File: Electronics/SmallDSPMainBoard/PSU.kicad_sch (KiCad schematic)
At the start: 17 parts, among them J15 Barrel_Jack_Switch

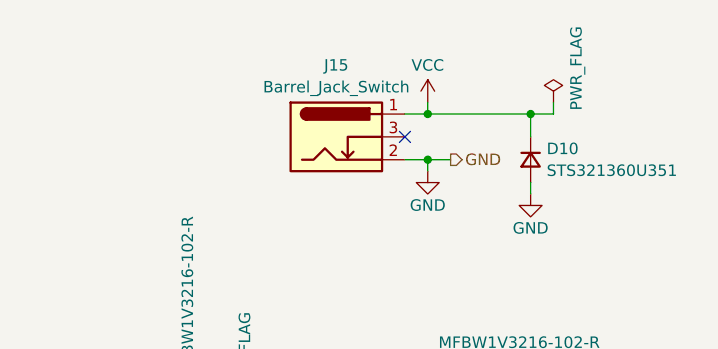
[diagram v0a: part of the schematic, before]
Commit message: Partly finishes layout
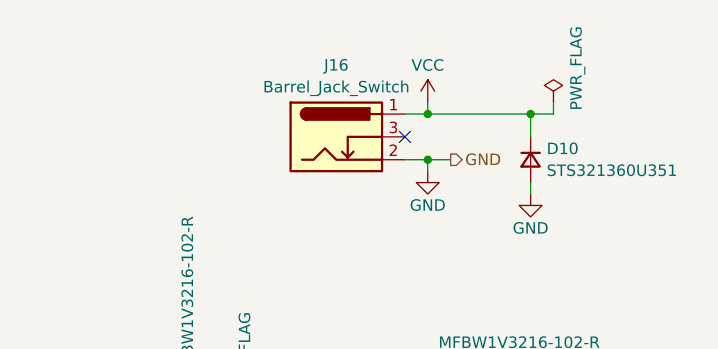
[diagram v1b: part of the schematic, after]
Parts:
- renumbered J15 to J16

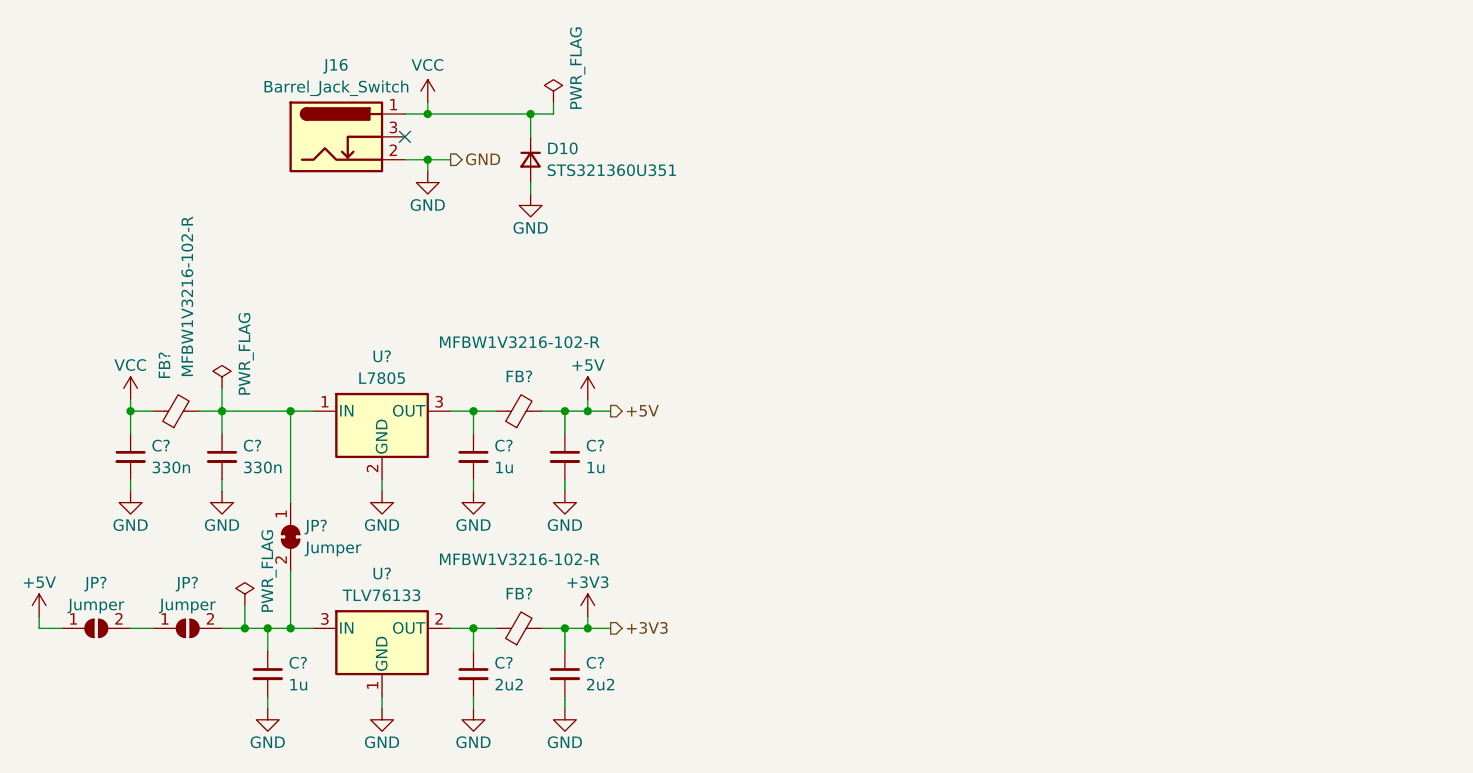
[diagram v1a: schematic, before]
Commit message: Finishes layout of Rev 1.0 and fixes a polarity error in the schematic
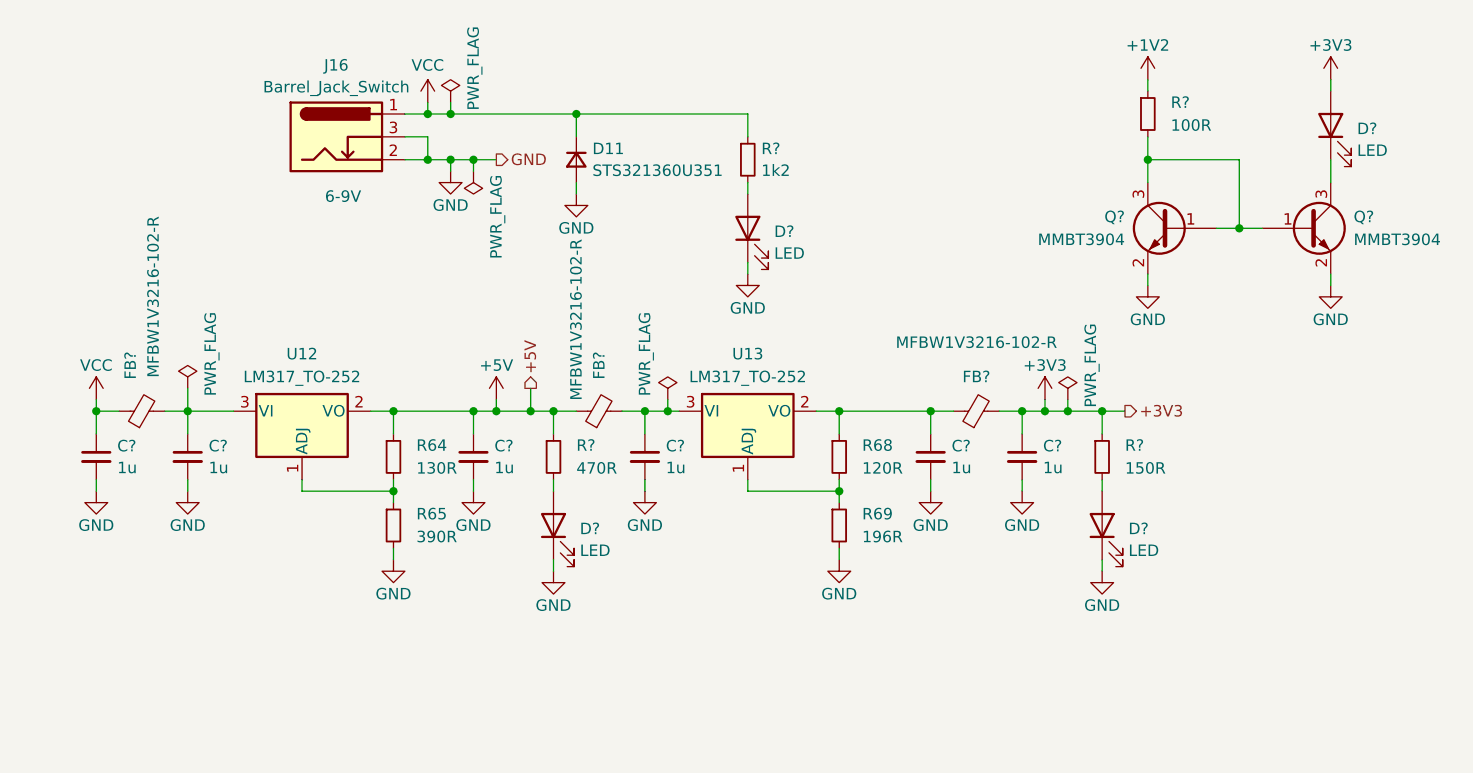
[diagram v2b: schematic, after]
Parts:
- removed C? (x2): 2u2, Capacitor_SMD:C_0603_1608Metric, symbol Device:C_Small
- removed C? (x2): 330n, Capacitor_SMD:C_0805_2012Metric, symbol Device:C_Small
- removed C?: 1u, Capacitor_SMD:C_0805_2012Metric, symbol Device:C_Small
- removed JP? (x2): Jumper, Jumper:SolderJumper-2_P1.3mm_Open_RoundedPad1.0x1.5mm, symbol Jumper:SolderJumper_2_Open
- removed JP?: Jumper, Jumper:SolderJumper-2_P1.3mm_Bridged_RoundedPad1.0x1.5mm, symbol Jumper:SolderJumper_2_Bridged
- removed U?: L7805, Package_TO_SOT_SMD:TO-252-2, symbol Regulator_Linear:L7805
- removed U?: TLV76133, Package_TO_SOT_SMD:SOT-223-3_TabPin2, symbol 1_Project_Symbols:TLV76133
- added C? (x4): 1u, Capacitor_SMD:C_0805_2012Metric, symbol Device:C_Small
- added D? (x4): LED, LED_SMD:LED_0603_1608Metric, symbol Device:LED
- added Q? (x2): MMBT3904, Package_TO_SOT_SMD:SOT-23, symbol Transistor_BJT:MMBT3904
- added R64: 130R, Resistor_SMD:R_0603_1608Metric_Pad0.98x0.95mm_HandSolder, symbol Device:R_Small
- added R65: 390R, Resistor_SMD:R_0603_1608Metric, symbol Device:R_Small
- added R68: 120R, Resistor_SMD:R_0402_1005Metric, symbol Device:R_Small
- added R69: 196R, Resistor_SMD:R_0603_1608Metric_Pad0.98x0.95mm_HandSolder, symbol Device:R_Small
- added R?: 1k2, Resistor_SMD:R_0402_1005Metric, symbol Device:R_Small
- added R?: 470R, Resistor_SMD:R_0402_1005Metric, symbol Device:R_Small
- added R?: 150R, Resistor_SMD:R_0402_1005Metric, symbol Device:R_Small
- added R?: 100R, Resistor_SMD:R_0402_1005Metric, symbol Device:R_Small
- added U12, U13: LM317_TO-252, Package_TO_SOT_SMD:TO-252-2, symbol Regulator_Linear:LM317_TO-252
- renumbered D10 to D11
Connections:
- net +3V3: now also C?.1, D?.2 (A), R?.1
- net +5V: now also C?.1, FB?.1, R64.1, R?.1, U12.2 (VO); no longer C?.1, FB?.2
- net GND: now also J16.3, C?.2, C?.2, C?.2, C?.2, D?.1 (K), D?.1 (K), D?.1 (K), Q?.2 (E), Q?.2 (E), R65.2, R69.2
- net VCC: now also C?.1, R?.1
- net at FB?.1: now also C?.1, R68.1, U13.2 (VO)
- net at FB?.2: now also C?.1, U12.3 (VI)
- new net: D?.2 (A), R?.2 (x3)
- new net: D?.1 (K), Q?.3 (C)
- new net: Q?.1 (B), Q?.1 (B), Q?.3 (C), R?.2
- new net: R68.2, R69.1, U13.1 (ADJ)
- new net: C?.1, FB?.2, U13.3 (VI)
- new net: R64.2, R65.1, U12.1 (ADJ)
- new net +1V2: R?.1
- no-connect marks 1 -> 0
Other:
- note added: "6-9V"
- moved on the sheet: C?, D11, FB?
